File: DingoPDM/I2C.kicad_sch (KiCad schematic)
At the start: 60 parts, among them U1 PCA9539, U2 MAX11613, U3 MAX11613, U4 PCA9539, U5 MB85RC256V, U6 MCP9808, U7 PCAL9554B, U8 PCA9635

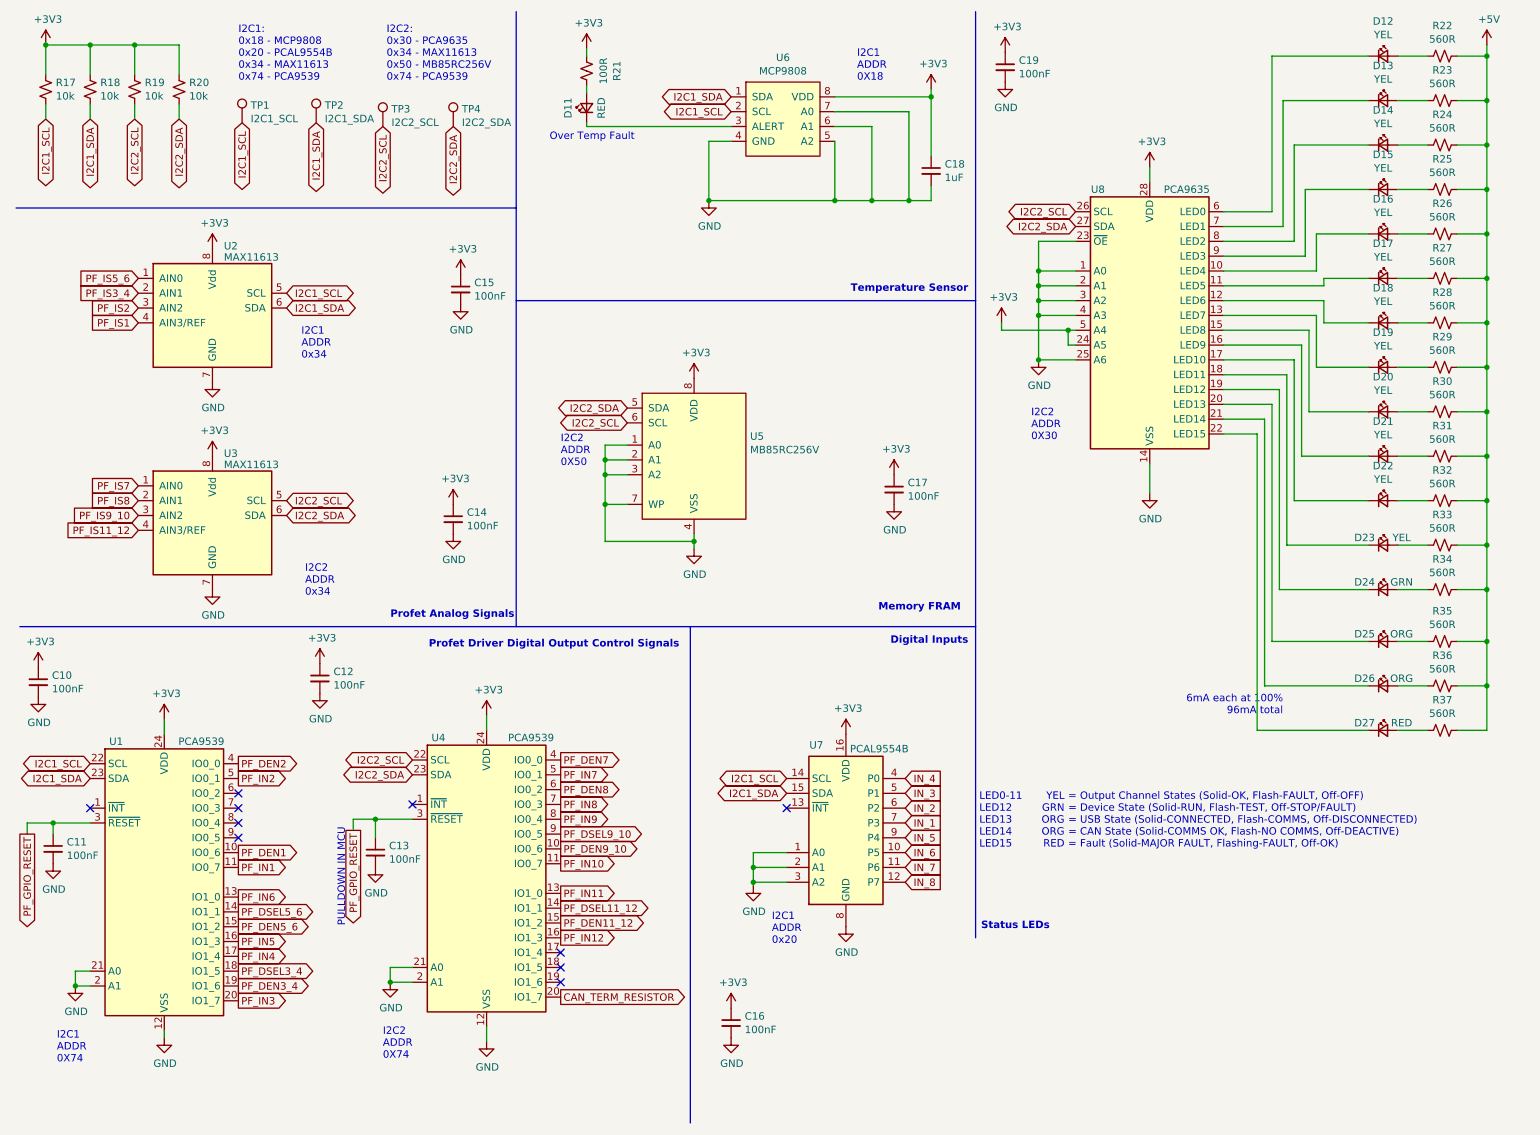
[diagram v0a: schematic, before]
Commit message: Redesigned to a smaller unit
4x high current, 2x med current, 4x low current, 2x digital inputs
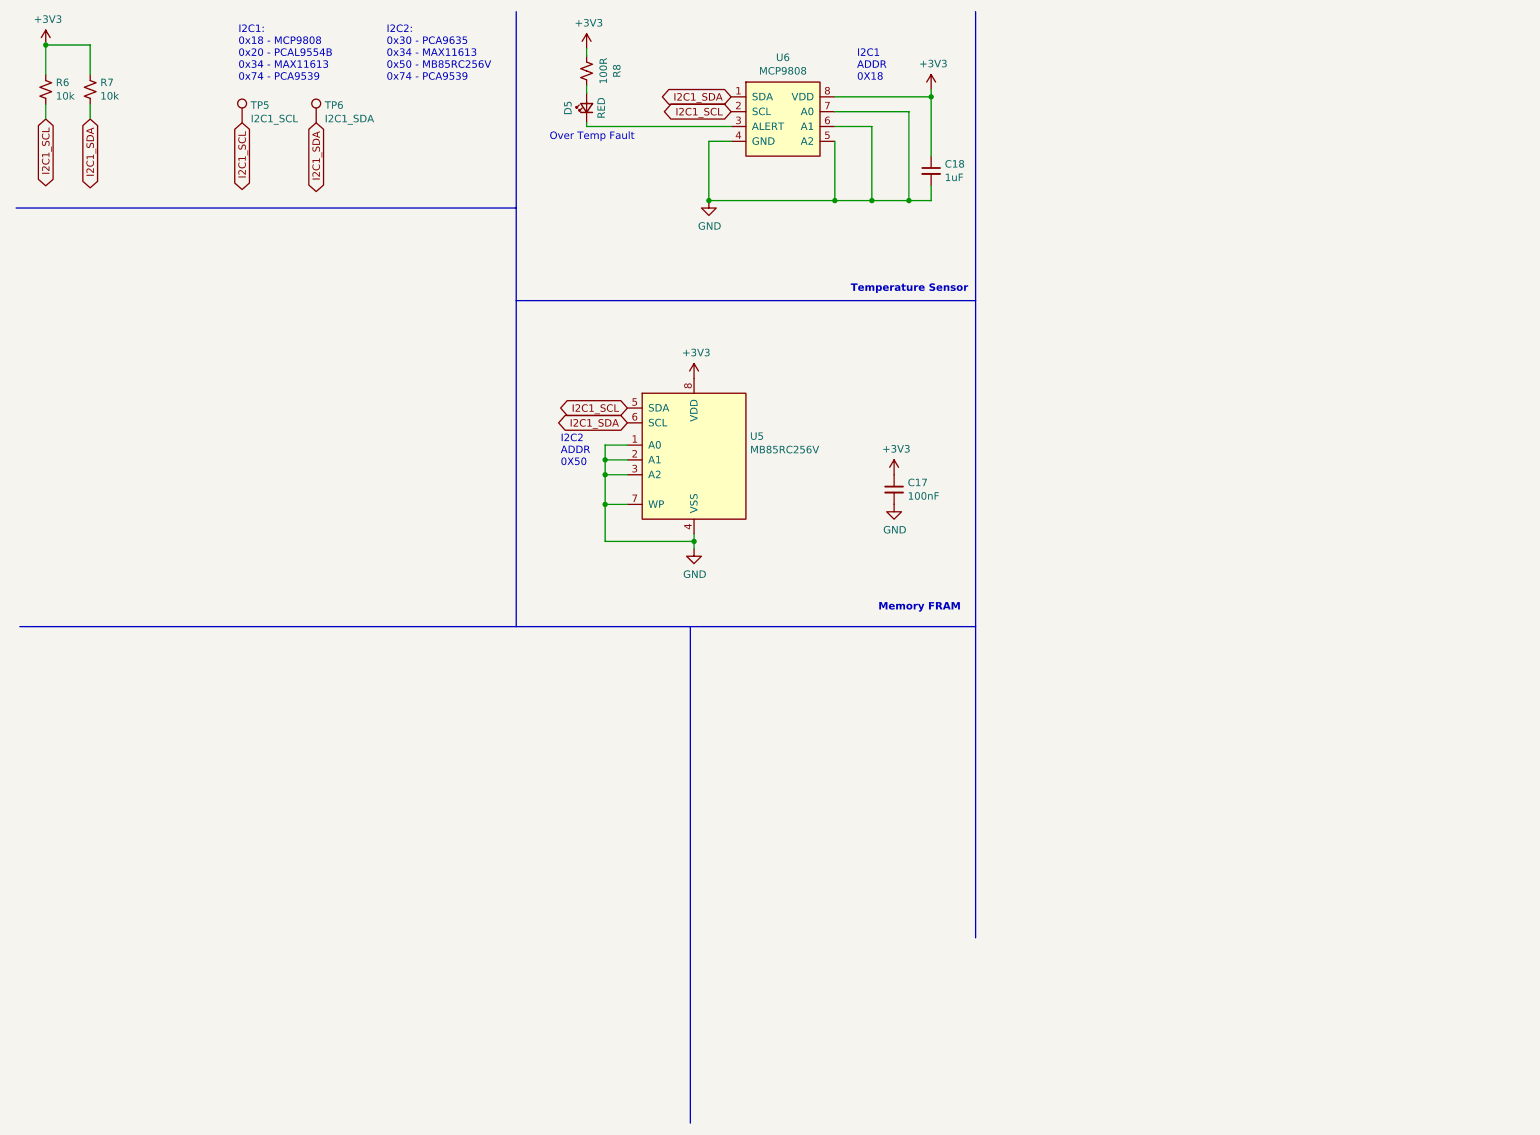
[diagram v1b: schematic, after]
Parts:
- removed C10, C11, C12, C13, C14, C15, C16, C19: 100nF, Capacitor_SMD:C_0805_2012Metric, symbol Device:C_Small
- removed D12, D13, D14, D15, D16, D17, D18, D19, D20, D21, D22, D23: YEL, LED_SMD:LED_0805_2012Metric, symbol Device:LED_Small
- removed D24: GRN, LED_SMD:LED_0805_2012Metric, symbol Device:LED_Small
- removed D25, D26: ORG, LED_SMD:LED_0805_2012Metric, symbol Device:LED_Small
- removed D27: RED, LED_SMD:LED_0805_2012Metric, symbol Device:LED_Small
- removed R19, R20: 10k, Resistor_SMD:R_0805_2012Metric, symbol Device:R_Small_US
- removed R22, R23, R24, R25, R26, R27, R28, R29, R30, R31, R32, R33, R34, R35, R36, R37: 560R, Resistor_SMD:R_0805_2012Metric, symbol Device:R_Small_US
- removed TP3: I2C2_SCL, TestPoint:TestPoint_Keystone_5000-5004_Miniature, symbol Connector:TestPoint
- removed TP4: I2C2_SDA, TestPoint:TestPoint_Keystone_5000-5004_Miniature, symbol Connector:TestPoint
- removed U1, U4: PCA9539, Package_SO:TSSOP-24_4.4x7.8mm_P0.65mm, symbol GPIO_Expansion:PCA9539
- removed U2, U3: MAX11613, Package_SO:MSOP-8_3x3mm_P0.65mm, symbol Analog_ADC:MAX11613
- removed U7: PCAL9554B, Package_SO:TSSOP-16_4.4x5mm_P0.65mm, symbol GPIO_Expansion:PCAL9554
- removed U8: PCA9635, Package_SO:TSSOP-28_4.4x9.7mm_P0.65mm, symbol Driver_LED:PCA9635
- C17: LCSC (none) -> C49678
- C18: LCSC (none) -> C28323
- R6: renamed from R17; LCSC (none) -> C17414
- R7: renamed from R18; LCSC (none) -> C17414
- U5: LCSC (none) -> C126728
- U6: LCSC (none) -> C129490
- renumbered D11 to D5, R21 to R8, TP1 to TP5, TP2 to TP6
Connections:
- net I2C2_SCL is gone; now on net I2C1_SDA: U5.6 (SCL)
- net I2C2_SDA is gone; now on net I2C1_SCL: U5.5 (SDA)
- no-connect marks 10 -> 0
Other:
- note removed: "6mA each at 100% 96mA total"
- note removed: "= Output Channel States (Solid-OK, Flash-FAULT, Off-OFF) = Device State (Solid-RUN, Flash-TEST, Off-STOP/FAULT) = USB State (Solid-CONNECTED, Flash-COMMS, Off-DISCONNECTED) = CAN State (Solid-COMMS OK, Flash-NO COMMS, Off-DEACTIVE) = Fault (Solid-MAJOR FAULT, Flashing-FAULT, Off-OK)"
- note removed: "Digital Inputs"
- note removed: "I2C1 ADDR 0X74"
- note removed: "I2C1 ADDR 0x20"
- note removed: "I2C1 ADDR 0x34"
- note removed: "I2C2 ADDR 0X30"
- note removed: "I2C2 ADDR 0X74"
- note removed: "I2C2 ADDR 0x34"
- note removed: "LED0-11 LED12 LED13 LED14 LED15"
- note removed: "PULLDOWN IN MCU"
- note removed: "Profet Analog Signals"
- note removed: "Profet Driver Digital Output Control Signals"
- note removed: "Status LEDs"
- note removed: "YEL GRN ORG ORG RED"

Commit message: Added documentation, finished and cleaned design
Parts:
- D5: LCSC (none) -> C2899997
- R8: value 100R -> 120R; Digi-Key_PN 311-100CRCT-ND -> 311-120CRCT-ND; LCSC (none) -> C229076
- U5: LCSC C126728 -> C47538
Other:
- note added: "I2C1: 0x18 - MCP9808 0x50 - MB85RC256V"
- note removed: "I2C1: 0x18 - MCP9808 0x20 - PCAL9554B 0x34 - MAX11613 0x74 - PCA9539"
- note removed: "I2C2: 0x30 - PCA9635 0x34 - MAX11613 0x50 - MB85RC256V 0x74 - PCA9539"
- moved on the sheet: C17, U5

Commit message: Small edits
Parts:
- R6, R7: value 10k -> 10K
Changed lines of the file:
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@@
       (effects (font (size 1.27 1.27)) (justify left))
     )
-    (property "Value" "10k" (at 18.8722 27.178 0)
+    (property "Value" "10K" (at 18.8722 27.178 0)
       (effects (font (size 1.27 1.27)) (justify left))
     )
@@
       (effects (font (size 1.27 1.27)) (justify left))
     )
-    (property "Value" "10k" (at 26.4922 27.178 0)
+    (property "Value" "10K" (at 26.4922 27.178 0)
       (effects (font (size 1.27 1.27)) (justify left))
     )

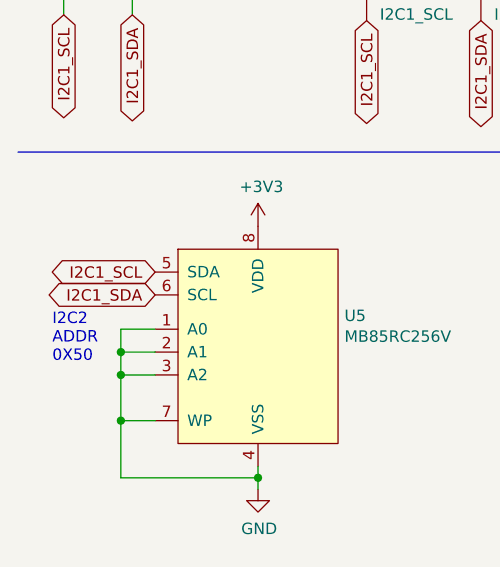
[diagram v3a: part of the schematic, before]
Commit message: V7.1 Fixes
SDA/SCL mixed up on FRAM, added status LEDs, switched to thermal relief zones
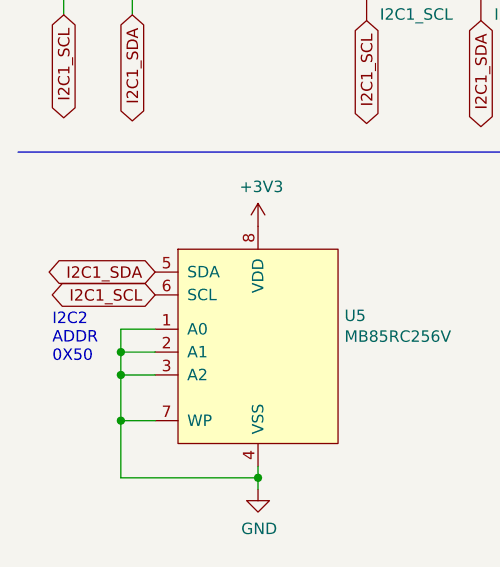
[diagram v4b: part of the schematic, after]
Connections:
- net I2C1_SCL: now also U5.6 (SCL); no longer U5.5 (SDA)
- net I2C1_SDA: now also U5.5 (SDA); no longer U5.6 (SCL)
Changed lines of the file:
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@@
   (title_block
     (title "Dingo_PDM")
-    (date "2023-07-28")
-    (rev "v6")
+    (date "2023-09-04")
+    (rev "v7.1")
     (comment 3 "github.com/corygrant")
     (comment 4 "Cory Grant")
@@
     (effects (font (size 1.27 1.27) (thickness 0.254) bold) (justify right bottom))
   )
-  (global_label "I2C1_SCL" (shape bidirectional) (at 27.305 59.69 180) (fields_autoplaced)
+  (global_label "I2C1_SCL" (shape bidirectional) (at 27.305 62.23 180) (fields_autoplaced)
     (effects (font (size 1.27 1.27)) (justify right))
-    (property "Intersheetrefs" "${INTERSHEET_REFS}" (at 15.3319 59.69 0)
+    (property "Intersheetrefs" "${INTERSHEET_REFS}" (at 15.3319 62.23 0)
       (effects (font (size 1.27 1.27)) (justify right) hide)
     )
@@
     )
   )
-  (global_label "I2C1_SDA" (shape bidirectional) (at 27.305 62.23 180) (fields_autoplaced)
+  (global_label "I2C1_SDA" (shape bidirectional) (at 27.305 59.69 180) (fields_autoplaced)
     (effects (font (size 1.27 1.27)) (justify right))
-    (property "Intersheetrefs" "${INTERSHEET_REFS}" (at 15.2714 62.23 0)
+    (property "Intersheetrefs" "${INTERSHEET_REFS}" (at 15.2714 59.69 0)
       (effects (font (size 1.27 1.27)) (justify right) hide)
     )
